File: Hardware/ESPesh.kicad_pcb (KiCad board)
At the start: 2 copper layers, 25.4 x 25.4 mm, 37 parts, among them IC1 ESP32-PICO-D4, IC3 FDN340P, U1 SPX3819M5-L-3-3, U2 SL4054ST25P, U3 XB6566H0, U4 HDC1080

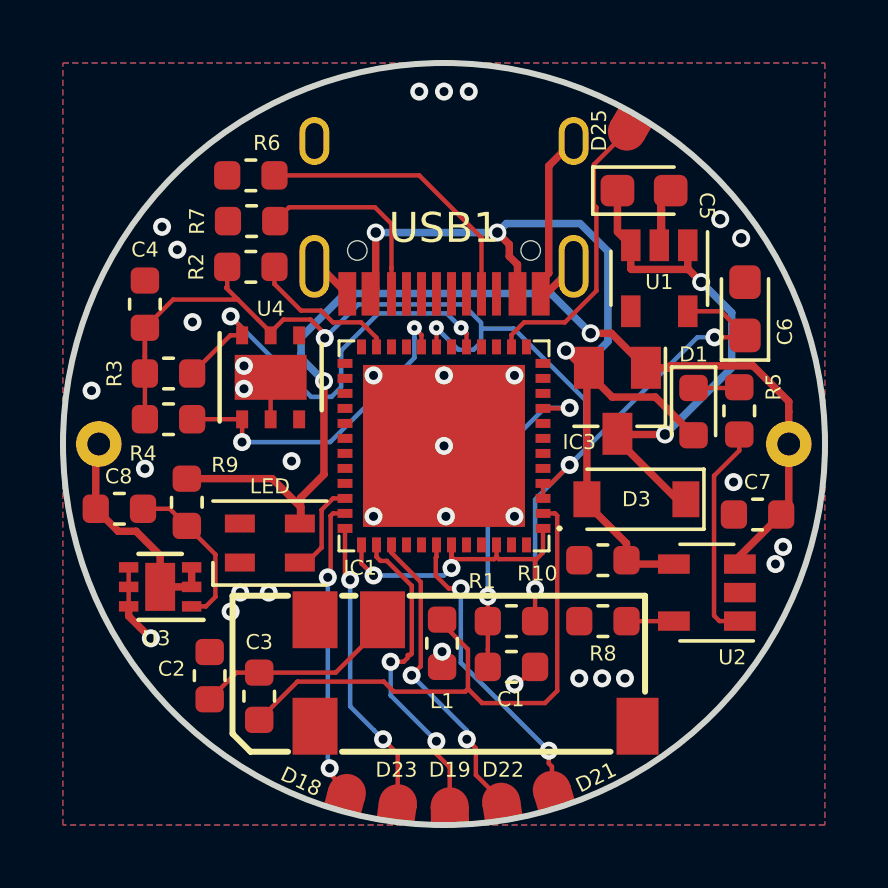
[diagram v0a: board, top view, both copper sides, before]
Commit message: Added GND pad
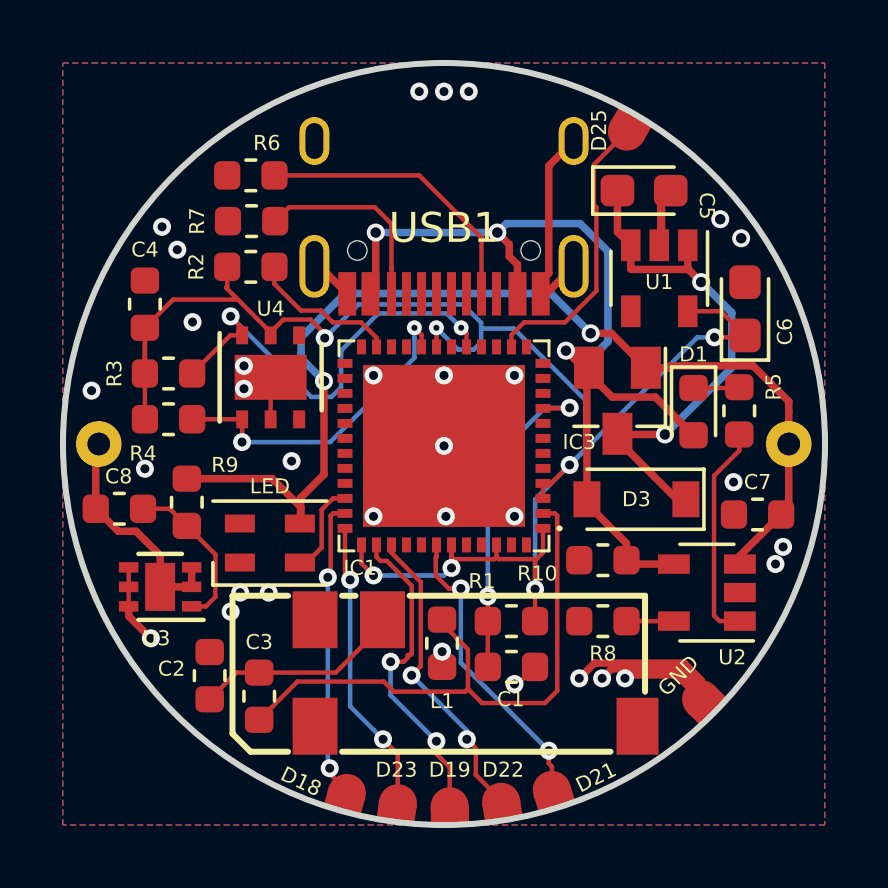
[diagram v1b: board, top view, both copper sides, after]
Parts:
- added GND: Conn_01x01, CustomFootprints:RoundPad, F.Cu at (161.7, 105.2)
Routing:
- net GND: track 18.5 -> 30.6 mm
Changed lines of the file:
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@@
     (thickness 1.6)
     (drawings 8)
-    (tracks 369)
+    (tracks 380)
     (zones 0)
-    (modules 37)
+    (modules 38)
     (nets 67)
   )
@@
     )
   )
+  (module CustomFootprints:RoundPad (layer F.Cu)
+    (at 161.671 105.2195 315)
+    (fp_text reference GND (at -1.095126 -0.017495 45) (layer F.SilkS)
+      (effects (font (size 0.5 0.5) (thickness 0.125)))
+    )
+    (fp_text value Conn_01x01 (at 0 -0.5 315) (layer F.Fab)
+      (effects (font (size 1 1) (thickness 0.15)))
+    )
+    (pad 1 smd custom (at 0 0 315) (size 1.27 1.27) (layers F.Cu F.Paste F.Mask)
+      (net 1 GND) (zone_connect 0)
+      (options (clearance outline) (anchor circle))
+      (primitives
+        (gr_poly (pts
+           (xy 0 0.635) (xy 0.635 0.635) (xy 0.635 -0.635) (xy 0 -0.635)) (width 0))
+      ))
+  )
   (gr_circle (center 153.0985 96.7105) (end 163.2585 89.0905) (layer Edge.Cuts) (width 0.2))
   (dimension 25.4 (width 0.3) (layer Dwgs.User)
@@
   (segment (start 156.3235 91.7055) (end 156.3235 91.2805) (width 0.25) (layer F.Cu) (net 1))
   (segment (start 156.3235 91.2805) (end 156.591 91.013) (width 0.25) (layer F.Cu) (net 1))
+  (segment (start 158.6865 104.2035) (end 158.369 104.521) (width 0.25) (layer F.Cu) (net 1))
+  (segment (start 160.9725 104.2035) (end 158.6865 104.2035) (width 0.25) (layer F.Cu) (net 1))
+  (segment (start 161.671 105.2195) (end 161.671 104.902) (width 0.25) (layer F.Cu) (net 1))
+  (segment (start 161.671 104.902) (end 160.9725 104.2035) (width 0.25) (layer F.Cu) (net 1))
+  (segment (start 158.115 104.013) (end 157.607 104.521) (width 0.25) (layer F.Cu) (net 1))
+  (segment (start 161.0995 104.013) (end 158.115 104.013) (width 0.25) (layer F.Cu) (net 1))
+  (segment (start 161.671 105.2195) (end 161.671 104.5845) (width 0.25) (layer F.Cu) (net 1))
+  (segment (start 161.671 104.5845) (end 161.0995 104.013) (width 0.25) (layer F.Cu) (net 1))
+  (segment (start 159.243059 104.408941) (end 159.131 104.521) (width 0.25) (layer F.Cu) (net 1))
+  (segment (start 161.671 105.2195) (end 160.860441 104.408941) (width 0.25) (layer F.Cu) (net 1))
+  (segment (start 160.860441 104.408941) (end 159.243059 104.408941) (width 0.25) (layer F.Cu) (net 1))
   (segment (start 154.3485 89.8325) (end 154.3485 91.7055) (width 0.15) (layer F.Cu) (net 4))
   (segment (start 147.447 87.757) (end 152.273 87.757) (width 0.15) (layer F.Cu) (net 4))
